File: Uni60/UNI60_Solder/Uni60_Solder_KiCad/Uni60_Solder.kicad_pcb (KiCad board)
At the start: 2 copper layers, 284.7 x 94.2 mm, 202 parts, among them J1 Conn_01x04, J2 Conn_01x04, J3 Conn_01x04, J4 Conn_01x04, J5 Conn_01x04, J6 Conn_01x04, SW1 SW_Push, SW2 SW_Push, U1 STM32F072CBTx, U2 XC6206PxxxMR, U3 USBLC6-2SC6

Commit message: fixed traces
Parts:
- moved J6 2.72 mm to (140.4, 89.6)
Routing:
- net /COL1: track 116.0 -> 113.7 mm
- net Net-(D28-A): track 38.8 -> 37.3 mm
- net /COL10: track 272.9 -> 271.8 mm
- net Net-(D59-A): track 23.8 -> 22.7 mm
- net Net-(D56-A): track 10.9 -> 9.77 mm
- net Net-(D40-A): track 7.17 -> 6.05 mm
- net Net-(D25-A): track 7.17 -> 6.05 mm
- net Net-(D51-A): track 7.17 -> 6.05 mm
- net Net-(D8-A): track 7.17 -> 6.05 mm
- net Net-(D36-A): track 7.17 -> 6.05 mm
- net Net-(D34-A): track 7.17 -> 6.05 mm
- net Net-(D31-A): track 7.17 -> 6.05 mm
- net Net-(D21-A): track 7.17 -> 6.05 mm
- net Net-(D19-A): track 7.17 -> 6.05 mm
- net Net-(D10-A): track 7.17 -> 6.05 mm
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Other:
- board text added: "Molex"

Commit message: final changes
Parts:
- moved C1 0.36 mm to (104.0, 112.6)
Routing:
- net GND: track 27.3 -> 27.4 mm, vias 29 -> 32
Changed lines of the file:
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@@
 	(footprint "shentobento:SW_MX_1u"
 		(layer "F.Cu")
-		(at 345.281227 106.997812 -90)
+		(at 345.281028 106.997604 -90)
 		(descr "Footprint for Cherry MX style switches")
 		(tags "cherry mx switch")
@@
 		)
 		(point
-			(at 335.756227 97.472812)
+			(at 335.756028 97.472604)
 			(size 1)
 			(layer "Dwgs.User")
 		)
 		(point
-			(at 335.756227 116.522812)
+			(at 335.756028 116.522604)
 			(size 1)
 			(layer "Dwgs.User")
 		)
 		(point
-			(at 345.281227 106.997812)
+			(at 345.281028 106.997604)
 			(size 1)
 			(layer "Dwgs.User")
 		)
 		(point
-			(at 354.806227 97.472812)
+			(at 354.806028 97.472604)
 			(size 1)
 			(layer "Dwgs.User")
 		)
 		(point
-			(at 354.806227 116.522812)
+			(at 354.806028 116.522604)
 			(size 1)
 			(layer "Dwgs.User")
@@
 	(footprint "shentobento:C_0201_0603Metric"
 		(layer "B.Cu")
-		(at 104.179668 112.950724)
+		(at 103.995688 112.635901)
 		(descr "Capacitor SMD 0201 (0603 Metric), square (rectangular) end terminal, IPC-7351 nominal, (Body size source: https://www.vishay.com/docs/20052/crcw0201e3.pdf)")
 		(tags "capacitor")
@@
 	)
 	(segment
+		(start 138.414796 99.258548)
+		(end 138.707764 99.258548)
+		(width 0.2)
+		(layer "B.Cu")
+		(net "/COL3")
+	)
+	(segment
 		(start 114.300028 103.425518)
 		(end 114.002158 103.723388)
@@
 	)
 	(segment
-		(start 114.002158 103.723388)
-		(end 108.346768 103.723388)
+		(start 136.624172 101.049172)
+		(end 138.414796 99.258548)
 		(width 0.2)
 		(layer "B.Cu")
@@
 	)
 	(segment
-		(start 172.40258 152.082436)
-		(end 160.496228 152.082436)
+		(start 114.002158 103.723388)
+		(end 108.346768 103.723388)
 		(width 0.2)
 		(layer "B.Cu")
@@
 	)
 	(segment
-		(start 138.707764 99.258548)
-		(end 136.91714 101.049172)
+		(start 172.40258 152.082436)
+		(end 160.496228 152.082436)
 		(width 0.2)
 		(layer "B.Cu")
@@
 	)
 	(via
-		(at 105.667948 111.462444)
+		(at 97.928892 107.890572)
 		(size 0.6)
 		(drill 0.3)
 		(layers "F.Cu" "B.Cu")
+		(free yes)
 		(net "GND")
 	)
 	(via
-		(at 131.266364 110.867132)
+		(at 105.667948 111.462444)
 		(size 0.6)
 		(drill 0.3)
@@
 	)
 	(via
-		(at 105.370292 112.653068)
+		(at 131.266364 110.867132)
 		(size 0.6)
 		(drill 0.3)
@@
 	)
 	(via
+		(at 100.31014 105.509324)
+		(size 0.6)
+		(drill 0.3)
+		(layers "F.Cu" "B.Cu")
+		(free yes)
+		(net "GND")
+	)
+	(via
 		(at 100.5325 115.1325)
 		(size 0.6)
@@
 	)
 	(via
+		(at 102.393732 107.592916)
+		(size 0.6)
+		(drill 0.3)
+		(layers "F.Cu" "B.Cu")
+		(free yes)
+		(net "GND")
+	)
+	(via
 		(at 139.600732 109.974164)
 		(size 0.6)
@@
 	)
 	(via
+		(at 105.072636 112.653068)
+		(size 0.6)
+		(drill 0.3)
+		(layers "F.Cu" "B.Cu")
+		(net "GND")
+	)
+	(via
 		(at 96.432375 91.074565)
 		(size 0.6)
@@
 	)
 	(via
-		(at 104.77498 103.128076)
+		(at 104.77498 103.425732)
 		(size 0.6)
 		(drill 0.3)
@@
 	)
 	(segment
-		(start 103.882012 102.51042)
-		(end 104.157324 102.51042)
-		(width 0.3)
-		(layer "B.Cu")
-		(net "GND")
-	)
-	(segment
 		(start 102.604209 101.771413)
 		(end 102.604209 101.962487)
@@
 	)
 	(segment
-		(start 105.370292 112.653068)
-		(end 105.072636 112.950724)
-		(width 0.3)
-		(layer "B.Cu")
-		(net "GND")
-	)
-	(segment
 		(start 102.36266 102.204036)
 		(end 102.36266 103.562623)
@@
 	)
 	(segment
-		(start 104.157324 102.51042)
-		(end 104.77498 103.128076)
+		(start 105.055469 112.635901)
+		(end 105.072636 112.653068)
 		(width 0.3)
 		(layer "B.Cu")
@@
 	)
 	(segment
+		(start 104.157324 102.51042)
+		(end 103.882012 102.51042)
+		(width 0.3)
+		(layer "B.Cu")
+		(net "GND")
+	)
+	(segment
 		(start 154.987916 86.526532)
 		(end 153.821028 86.526532)
@@
 	)
 	(segment
+		(start 104.315688 112.635901)
+		(end 105.055469 112.635901)
+		(width 0.3)
+		(layer "B.Cu")
+		(net "GND")
+	)
+	(segment
 		(start 132.248396 110.890572)
 		(end 131.289804 110.890572)
@@
 	)
 	(segment
-		(start 105.072636 112.950724)
-		(end 104.499668 112.950724)
+		(start 138.251516 109.421356)
+		(end 139.047924 109.421356)
 		(width 0.3)
 		(layer "B.Cu")
@@
 	)
 	(segment
-		(start 138.251516 109.421356)
-		(end 139.047924 109.421356)
+		(start 139.047924 109.421356)
+		(end 139.600732 109.974164)
 		(width 0.3)
 		(layer "B.Cu")
@@
 	)
 	(segment
-		(start 139.047924 109.421356)
-		(end 139.600732 109.974164)
+		(start 104.77498 103.128076)
+		(end 104.157324 102.51042)
 		(width 0.3)
 		(layer "B.Cu")
@@
 	)
 	(segment
+		(start 104.77498 103.425732)
+		(end 104.77498 103.128076)
+		(width 0.3)
+		(layer "B.Cu")
+		(net "GND")
+	)
+	(segment
 		(start 98.868533 114.692533)
 		(end 98.868533 113.978492)
@@
 	)
 	(segment
+		(start 103.675688 112.635901)
+		(end 103.610938 112.635901)
+		(width 0.3)
+		(layer "B.Cu")
+		(net "+3.3V")
+	)
+	(segment
 		(start 104.27516 110.475123)
 		(end 103.192347 110.475123)
@@
 	)
 	(segment
+		(start 103.610938 112.635901)
+		(end 102.86266 111.887623)
+		(width 0.3)
+		(layer "B.Cu")
+		(net "+3.3V")
+	)
+	(segment
 		(start 95.788268 101.88042)
 		(end 95.867644 101.959796)
@@
 	)
 	(segment
-		(start 103.859668 112.884631)
-		(end 102.86266 111.887623)
-		(width 0.3)
-		(layer "B.Cu")
-		(net "+3.3V")
-	)
-	(segment
 		(start 103.192347 110.475123)
 		(end 100.161312 107.444088)
@@
 	)
 	(segment
-		(start 138.410108 88.071493)
-		(end 135.731204 88.071493)
+		(start 117.360124 88.071493)
+		(end 138.410108 88.071493)
 		(width 0.3)
 		(layer "B.Cu")
@@
 	)
 	(segment
-		(start 135.731204 88.071493)
-		(end 117.360124 88.071493)
-		(width 0.3)
-		(layer "B.Cu")
-		(net "+5V")
-	)
-	(segment
 		(start 100.201947 101.531603)
 		(end 99.551898 100.881554)
@@
 	)
 	(segment
-		(start 135.731204 89.071493)
+		(start 117.360124 89.071493)
 		(end 144.429979 89.071493)
 		(width 0.3)
@@
 	)
 	(segment
-		(start 117.360124 89.071493)
-		(end 135.731204 89.071493)
-		(width 0.3)
-		(layer "B.Cu")
-		(net "/USB_D-")
-	)
-	(segment
 		(start 100.883169 89.942178)
 		(end 100.012484 89.071493)
@@
 	)
 	(segment
-		(start 117.360124 90.071493)
-		(end 135.731204 90.071493)
-		(width 0.3)
-		(layer "B.Cu")
-		(net "/USB_D+")
-	)
-	(segment
 		(start 99.972203 90.071493)
 		(end 100.012484 90.031212)
@@
 	)
 	(segment
-		(start 135.731204 90.071493)
+		(start 117.360124 90.071493)
 		(end 144.918259 90.071493)
 		(width 0.3)

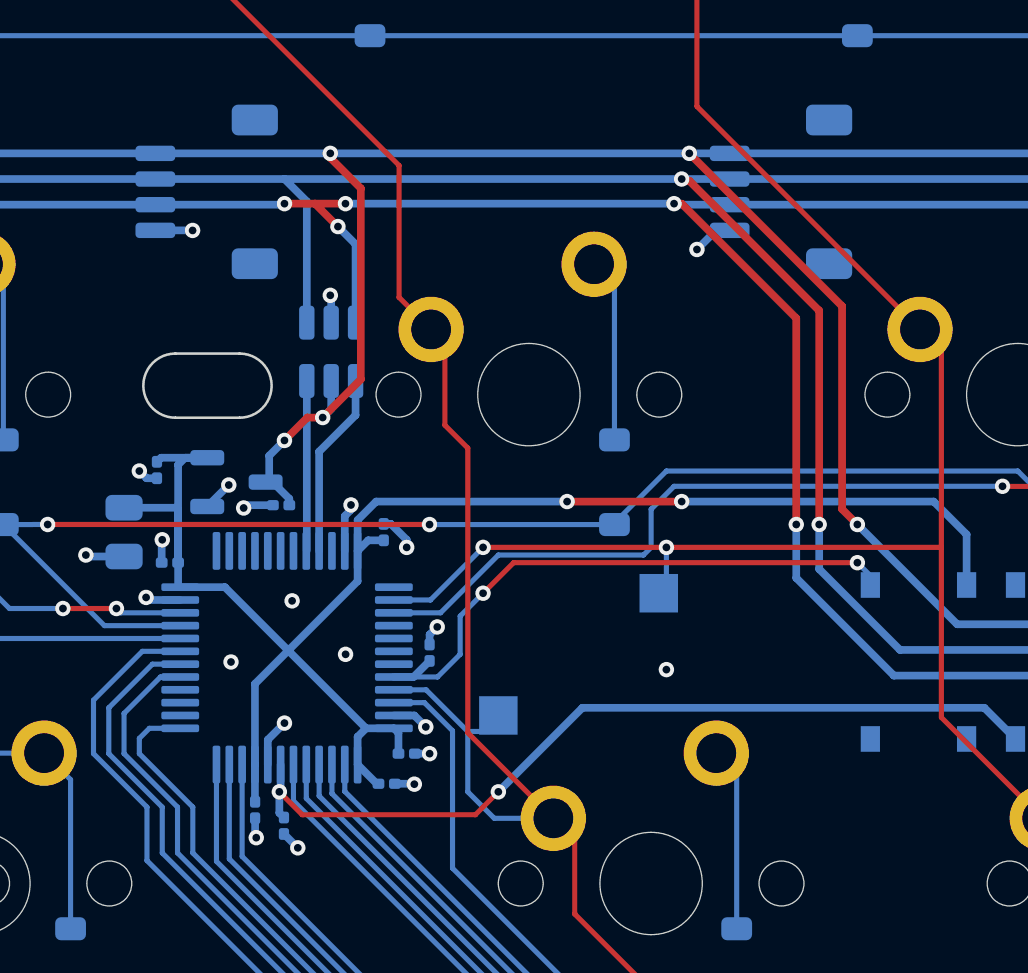
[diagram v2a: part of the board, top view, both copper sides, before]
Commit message: added alps footprints
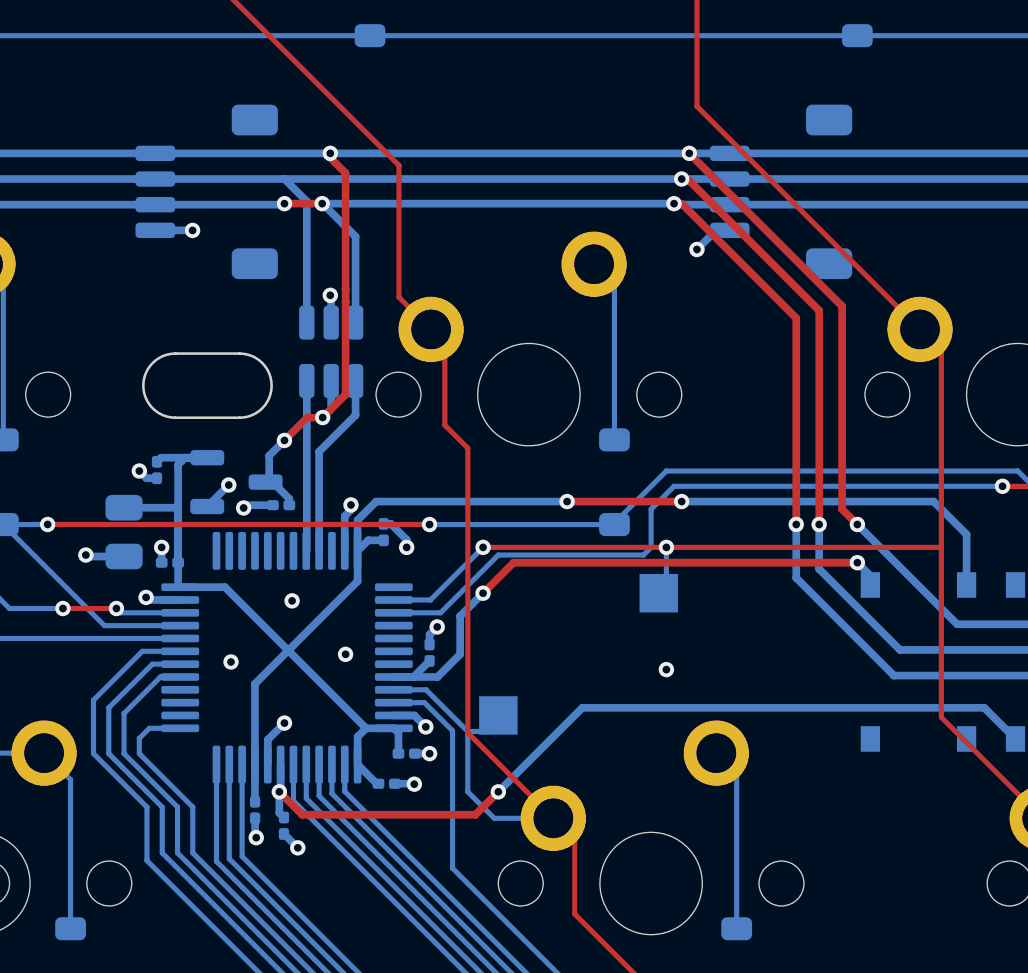
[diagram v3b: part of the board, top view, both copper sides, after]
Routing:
- net /USB_D+: track 139.1 -> 139.0 mm, vias 5 -> 4
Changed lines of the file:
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@@
 		(start 107.453732 113.843692)
 		(end 100.705628 113.843692)
-		(width 0.2)
+		(width 0.3)
 		(layer "F.Cu")
 		(net "/NRST")
@@
 		(start 100.705628 113.843692)
 		(end 99.81266 112.950724)
-		(width 0.2)
+		(width 0.3)
 		(layer "F.Cu")
 		(net "/NRST")
@@
 		(start 108.346898 112.950526)
 		(end 107.453732 113.843692)
-		(width 0.2)
+		(width 0.3)
 		(layer "F.Cu")
 		(net "/NRST")
@@
 	)
 	(via
-		(at 95.249988 103.128076)
+		(at 95.227644 103.425732)
 		(size 0.6)
 		(drill 0.3)
@@
 	)
 	(segment
-		(start 95.227644 103.15042)
-		(end 95.227644 104.021044)
-		(width 0.3)
-		(layer "B.Cu")
-		(net "GND")
-	)
-	(segment
 		(start 105.073595 109.975123)
 		(end 104.27516 109.975123)
@@
 	)
 	(segment
-		(start 95.249988 103.128076)
-		(end 95.227644 103.15042)
-		(width 0.3)
-		(layer "B.Cu")
-		(net "GND")
-	)
-	(segment
 		(start 138.251516 109.421356)
 		(end 139.047924 109.421356)
@@
 	)
 	(segment
+		(start 95.227644 103.425732)
+		(end 95.227644 104.021044)
+		(width 0.3)
+		(layer "B.Cu")
+		(net "GND")
+	)
+	(segment
 		(start 77.702976 108.694724)
 		(end 77.702976 107.309952)
@@
 	)
 	(segment
-		(start 102.989044 89.4359)
+		(start 102.393732 88.840588)
 		(end 101.79842 88.245276)
 		(width 0.3)
@@
 	)
 	(segment
+		(start 102.393732 93.349867)
+		(end 102.393732 88.840588)
+		(width 0.3)
+		(layer "F.Cu")
+		(net "+5V")
+	)
+	(segment
+		(start 102.39842 93.354555)
+		(end 102.393732 93.349867)
+		(width 0.3)
+		(layer "F.Cu")
+		(net "+5V")
+	)
+	(segment
 		(start 115.788252 88.071493)
 		(end 121.741372 94.024613)
@@
 	)
 	(segment
+		(start 102.393732 93.856301)
+		(end 102.39842 93.851613)
+		(width 0.3)
+		(layer "F.Cu")
+		(net "+5V")
+	)
+	(segment
+		(start 102.393732 97.472612)
+		(end 102.393732 93.856301)
+		(width 0.3)
+		(layer "F.Cu")
+		(net "+5V")
+	)
+	(segment
 		(start 101.79842 88.245276)
 		(end 101.79842 88.071493)
@@
 	)
 	(segment
-		(start 102.989044 96.8773)
-		(end 102.989044 89.4359)
+		(start 102.39842 93.851613)
+		(end 102.39842 93.354555)
 		(width 0.3)
 		(layer "F.Cu")
@@
 	(segment
 		(start 101.500764 98.36558)
-		(end 102.989044 96.8773)
+		(end 102.393732 97.472612)
 		(width 0.3)
 		(layer "F.Cu")
@@
 	)
 	(segment
-		(start 100.012484 90.031212)
-		(end 101.203108 90.031212)
-		(width 0.3)
-		(layer "F.Cu")
-		(net "/USB_D+")
-	)
-	(segment
-		(start 102.096076 90.92418)
-		(end 101.203108 90.031212)
-		(width 0.3)
-		(layer "F.Cu")
-		(net "/USB_D+")
-	)
-	(segment
 		(start 115.19294 90.031212)
 		(end 115.490596 90.031212)
@@
 	)
 	(segment
-		(start 101.203108 90.031212)
-		(end 102.389044 90.031212)
+		(start 101.483169 90.031212)
+		(end 100.012484 90.031212)
 		(width 0.3)
 		(layer "F.Cu")
@@
 	)
 	(via
-		(at 102.096076 90.92418)
+		(at 119.955436 102.532764)
 		(size 0.6)
 		(drill 0.3)
@@
 	)
 	(via
-		(at 119.955436 102.532764)
+		(at 100.012484 90.031212)
 		(size 0.6)
 		(drill 0.3)
@@
 	)
 	(via
-		(at 100.012484 90.031212)
-		(size 0.6)
-		(drill 0.3)
-		(layers "F.Cu" "B.Cu")
-		(net "/USB_D+")
-	)
-	(via
-		(at 102.389044 90.031212)
+		(at 101.483169 90.031212)
 		(size 0.6)
 		(drill 0.3)
@@
 	)
 	(segment
+		(start 101.483169 90.031212)
+		(end 101.500764 90.031212)
+		(width 0.3)
+		(layer "B.Cu")
+		(net "/USB_D+")
+	)
+	(segment
 		(start 144.918259 90.071493)
 		(end 149.46322 85.526532)
@@
 	)
 	(segment
-		(start 102.096076 90.92418)
-		(end 102.783169 91.611273)
-		(width 0.3)
-		(layer "B.Cu")
-		(net "/USB_D+")
-	)
-	(segment
 		(start 76.702976 92.802456)
 		(end 76.702976 108.694724)
@@
 	)
 	(segment
-		(start 102.783169 91.611273)
-		(end 102.783169 94.667368)
-		(width 0.3)
-		(layer "B.Cu")
-		(net "/USB_D+")
-	)
-	(segment
 		(start 117.360124 90.071493)
 		(end 144.918259 90.071493)
@@
 	)
 	(segment
-		(start 102.389044 90.031212)
+		(start 101.483169 90.031212)
 		(end 115.19294 90.031212)
+		(width 0.3)
+		(layer "B.Cu")
+		(net "/USB_D+")
+	)
+	(segment
+		(start 101.500764 90.031212)
+		(end 102.783169 91.313617)
 		(width 0.3)
 		(layer "B.Cu")
@@
 	)
 	(segment
+		(start 102.783169 91.313617)
+		(end 102.783169 94.667368)
+		(width 0.3)
+		(layer "B.Cu")
+		(net "/USB_D+")
+	)
+	(segment
 		(start 122.336684 104.021044)
 		(end 108.942164 104.021044)
-		(width 0.2)
+		(width 0.3)
 		(layer "F.Cu")
 		(net "/BOOT0")
@@
 		(start 108.942164 104.021044)
 		(end 107.75154 105.211668)
-		(width 0.2)
+		(width 0.3)
 		(layer "F.Cu")
 		(net "/BOOT0")
@@
 		(start 106.858572 106.104636)
 		(end 106.858572 107.592916)
-		(width 0.2)
+		(width 0.3)
 		(layer "B.Cu")
 		(net "/BOOT0")
@@
 		(start 122.842932 104.527292)
 		(end 122.336684 104.021044)
-		(width 0.2)
+		(width 0.3)
 		(layer "B.Cu")
 		(net "/BOOT0")
@@
 		(start 106.858572 107.592916)
 		(end 105.976365 108.475123)
-		(width 0.2)
+		(width 0.3)
 		(layer "B.Cu")
 		(net "/BOOT0")
@@
 		(start 107.75154 105.211668)
 		(end 106.858572 106.104636)
-		(width 0.2)
+		(width 0.3)
 		(layer "B.Cu")
 		(net "/BOOT0")
@@
 		(start 105.976365 108.475123)
 		(end 104.27516 108.475123)
-		(width 0.2)
+		(width 0.3)
 		(layer "B.Cu")
 		(net "/BOOT0")
@@
 			)
 		)
-	)
-	(zone
-		(layer "B.Cu")
-		(name "top right gnd")
-		(hatch edge 0.5)
-		(connect_pads
-			(clearance 0)
-		)
-		(min_thickness 0.25)
-		(keepout
-			(tracks allowed)
-			(vias allowed)
-			(pads allowed)
-			(copperpour not_allowed)
-			(footprints allowed)
-		)
-		(placement
-			(enabled no)
-			(sheetname "")
-		)
-		(fill
-			(thermal_gap 0.5)
-			(thermal_bridge_width 0.5)
-			(island_removal_mode 0)
-		)
-		(polygon
-			(pts
-				(xy 94.654676 103.425732) (xy 92.86874 102.235108) (xy 92.86874 105.80698) (xy 96.142956 105.80698)
-			)
-		)
